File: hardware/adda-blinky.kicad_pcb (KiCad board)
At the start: 2 copper layers, 46.2 x 35.1 mm, 17 parts, among them J1 Conn_01x02, J2 Conn_01x02, J3 USB_B_Micro, J4 Conn_01x02, U1 ATtiny1616-S, U2 ATtiny1616-M, U3 AMS1117-3.3

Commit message: First order
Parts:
- removed C2: 1u, Capacitor_SMD:C_0805_2012Metric
- removed U1: ATtiny1616-S, Package_SO:SOIC-20W_7.5x12.8mm_P1.27mm
- removed U3: AMS1117-3.3, Package_TO_SOT_SMD:SOT-223-3_TabPin2
- added C5: 1u, Capacitor_SMD:C_0805_2012Metric, F.Cu at (120.9, 52.1)
- added D10: 1N5819, Diode_SMD:D_SOD-323, F.Cu at (120.9, 50.0)
- added H1: MountingHole, MountingHole:MountingHole_3.2mm_M3_Pad, F.Cu at (92.7, 41.9)
- added H2: MountingHole, MountingHole:MountingHole_3.2mm_M3_Pad, F.Cu at (92.7, 72.4)
- added H3: MountingHole, MountingHole:MountingHole_3.2mm_M3_Pad, F.Cu at (135.9, 72.4)
- added H4: MountingHole, MountingHole:MountingHole_3.2mm_M3_Pad, F.Cu at (135.9, 41.9)
- added J5: PWR, Connector_Molex:Molex_KK-254_AE-6410-03A_1x03_P2.54mm_Vertical, F.Cu at (123.2, 41.9)
- added R0: 220, Resistor_SMD:R_0805_2012Metric, F.Cu at (121.9, 67.6)
- added R1: 220, Resistor_SMD:R_0805_2012Metric, F.Cu at (119.9, 67.6)
- added R2: 220, Resistor_SMD:R_0805_2012Metric, F.Cu at (117.9, 67.6)
- added R3: 220, Resistor_SMD:R_0805_2012Metric, F.Cu at (115.8, 67.6)
- added R4: 220, Resistor_SMD:R_0805_2012Metric, F.Cu at (113.8, 67.6)
- added R5: 220, Resistor_SMD:R_0805_2012Metric, F.Cu at (111.7, 67.6)
- added R6: 220, Resistor_SMD:R_0805_2012Metric, F.Cu at (109.7, 67.6)
- added R7: 220, Resistor_SMD:R_0805_2012Metric, F.Cu at (107.7, 67.6)
- added R8: 220, Resistor_SMD:R_0805_2012Metric, F.Cu at (125.9, 50.0)
- added RV1: R_Potentiometer, Connector_PinHeader_2.54mm:PinHeader_1x03_P2.54mm_Vertical, F.Cu at (132.1, 48.3)
- J1: value Conn_01x02 -> AIN
- J2: value Conn_01x02 -> AOUT
- J3: value USB_B_Micro -> PB5; footprint Connector_USB:USB_Micro-AB_Molex_47590-0001 -> Connector_Molex:Molex_KK-254_AE-6410-02A_1x02_P2.54mm_Vertical
- J4: value Conn_01x02 -> COMM; footprint Connector_Molex:Molex_KK-254_AE-6410-02A_1x02_P2.54mm_Vertical -> Connector_Molex:Molex_KK-254_AE-6410-05A_1x05_P2.54mm_Vertical
- moved J2 32.1 mm to (135.9, 59.7), turned to -90 degrees
- moved J3 29.4 mm to (115.6, 41.9), turned to 0 degrees
- moved J1 12.3 mm to (92.7, 62.2)
- moved U2 11.8 mm to (115.6, 53.3)
- moved C1 11.4 mm to (125.9, 52.1), turned to 180 degrees
- moved J4 10.7 mm to (100.3, 41.9), turned to 0 degrees
- moved D2 7.39 mm to (117.9, 71.1)
- moved D3 7.39 mm to (115.9, 71.1)
- moved D6 7.39 mm to (109.8, 71.1)
- moved D7 7.39 mm to (107.7, 71.1)
- moved D4 7.39 mm to (113.8, 71.1)
- moved D5 7.39 mm to (111.8, 71.1)
- moved D0 7.38 mm to (121.9, 71.1)
- moved D1 7.38 mm to (119.9, 71.1)
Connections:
- C1 pad 1: +3.3V -> /PB4
- D0 pad 1: /PC0 -> Net-(D0-K)
- D0 pad 2: +3.3V -> +5V
- D1 pad 1: /PC1 -> Net-(D1-K)
- D1 pad 2: +3.3V -> +5V
- D2 pad 1: /PC2 -> Net-(D2-K)
- D2 pad 2: +3.3V -> +5V
- D3 pad 1: /PC3 -> Net-(D3-K)
- D3 pad 2: +3.3V -> +5V
- D4 pad 1: /PB0 -> Net-(D4-K)
- D4 pad 2: +3.3V -> +5V
- D5 pad 1: /PB1 -> Net-(D5-K)
- D5 pad 2: +3.3V -> +5V
- D6 pad 1: /PB2 -> Net-(D6-K)
- D6 pad 2: +3.3V -> +5V
- D7 pad 1: /PB3 -> Net-(D7-K)
- D7 pad 2: +3.3V -> +5V
- J1 pad 1: /PA5/AIN5 -> GND
- J1 pad 2: GND -> /PA5/AIN5
- J3 pad 1: Net-(D8-A) -> GND
- J3 pad 2: unconnected-(J3-D--Pad2) -> /PB5
- J4 pad 1: +VDC -> GND
- J4 pad 2: GND -> /PA4/SS
- U2 pad 4: +3.3V -> +5V
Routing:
- net +5V: track 0.00 -> 60.0 mm, vias 0 -> 2
- net /PA6/OUT: track 3.82 -> 30.1 mm, vias 0 -> 2
- net /PB4: track 3.76 -> 24.2 mm, vias 0 -> 2
- net /PA5/AIN5: track 4.46 -> 24.4 mm
- net /PB5: track 3.42 -> 17.7 mm, vias 0 -> 4
- net /PA4/SS: track 5.72 -> 18.3 mm
- net /PA3/SCK: track 5.69 -> 16.6 mm
- net /PA1/MOSI/SDA: track 3.55 -> 13.6 mm
- net /PA2/MISO/SCL: track 4.59 -> 14.5 mm
- net /~{RESET}: track 3.19 -> 12.7 mm, vias 0 -> 2
- net /UPDI: track 0.00 -> 8.74 mm
- net Net-(D10-A): track 0.00 -> 8.65 mm
- net +3.3V: track 7.77 -> 0.00 mm
- net GND: track 10.9 -> 5.69 mm
- net /PA7: track 3.46 -> 0.00 mm
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- added copper zone on B.Cu, net GND
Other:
- board size 46.2 x 35.1 mm -> 50.8 x 38.1 mm
- board text added: "0"
- board text added: "1"
- board text added: "2"
- board text added: "3"
- board text added: "4"
- board text added: "5"
- board text added: "6"
- board text added: "7"
- board text added: "ADC"
- board text added: "DAC"
- board text added: "GND"
- board text added: "PA1/MOSI/SDA"
- board text added: "PA2/MISO/SCL"
- board text added: "PA3/SCK"
- board text added: "PA4/SS"
- board text added: "PB5"
- board text added: "UPDI"
- board text added: "VDD"
- board text added: "Vin"
- board text added: "Vout"

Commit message: Add series resistors to I/Os
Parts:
- added R10: 220, Resistor_SMD:R_0805_2012Metric, F.Cu at (135.5, 57.1)
- added R9: 220, Resistor_SMD:R_0805_2012Metric, F.Cu at (93.0, 57.1)
- moved J1 1.27 mm to (92.7, 63.5)
- moved J2 1.27 mm to (135.9, 61.0)
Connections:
- J1 pad 2: /PA5/AIN5 -> Net-(J1-Pin_2)
- J2 pad 1: /PA6/OUT -> Net-(J2-Pin_1)
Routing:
- net Net-(J1-Pin_2): track 0.00 -> 4.08 mm
- net Net-(J2-Pin_1): track 0.00 -> 4.03 mm
- net /PB3: track 15.0 -> 17.6 mm
- net /PA6/OUT: track 30.1 -> 27.7 mm
- net /PB2: track 14.1 -> 16.0 mm
- net /PA5/AIN5: track 24.4 -> 22.5 mm
- net GND: track 5.69 -> 7.03 mm, vias 3 -> 4
- net /PB1: track 13.5 -> 14.4 mm
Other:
- board text added: "8b"

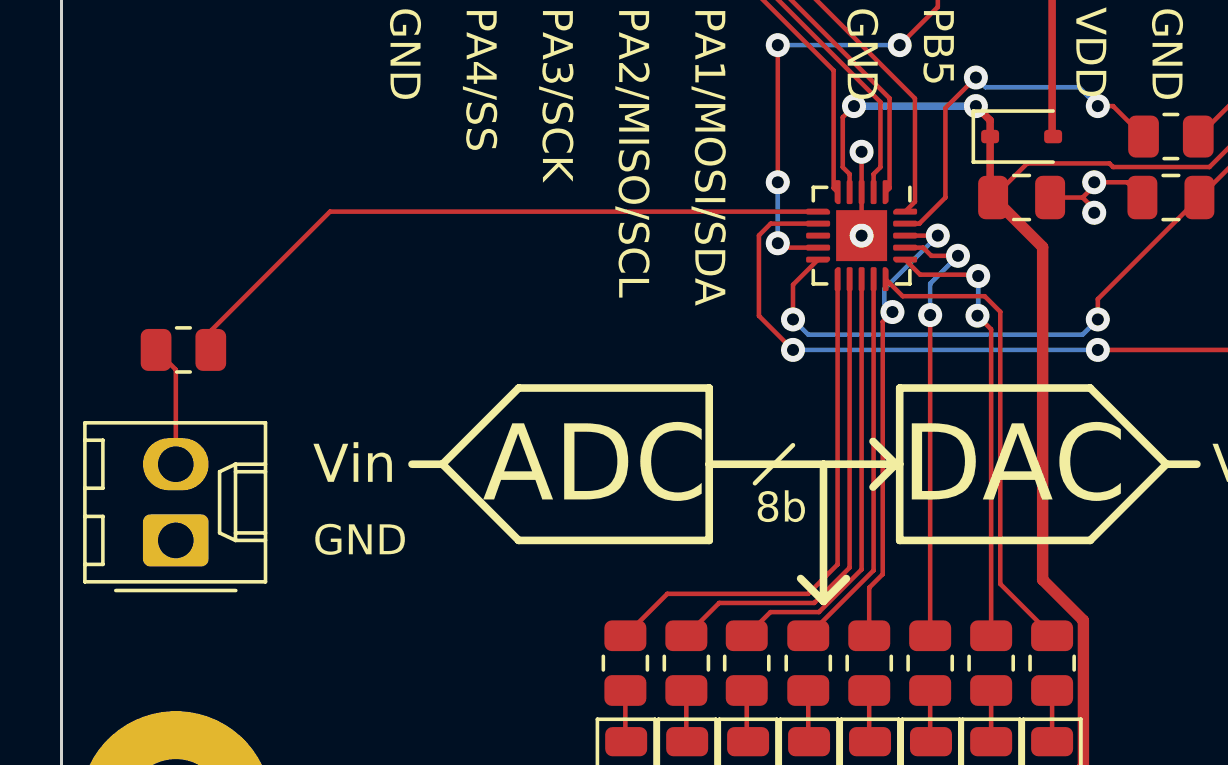
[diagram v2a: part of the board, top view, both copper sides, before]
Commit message: Add LED to PB5 for status and sample indicator
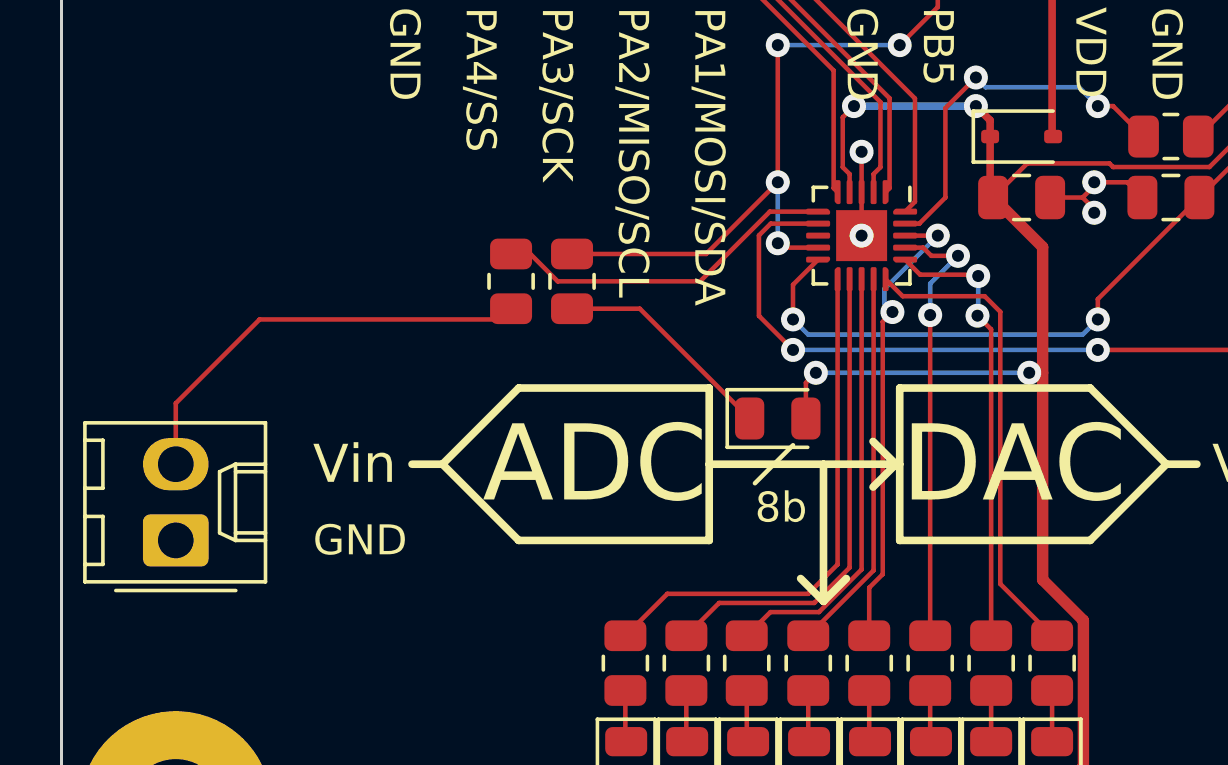
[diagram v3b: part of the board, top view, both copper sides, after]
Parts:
- added D8: LED, Diode_SMD:D_0805_2012Metric, F.Cu at (112.8, 59.4)
- added R11: 220, Resistor_SMD:R_0805_2012Metric, F.Cu at (105.9, 54.9)
- RV1: value R_Potentiometer -> FS
- moved R9 11.2 mm to (103.9, 54.9), turned to 90 degrees
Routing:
- net /PA5/AIN5: track 22.5 -> 11.6 mm
- net Net-(J1-Pin_2): track 4.08 -> 14.5 mm
- net +5V: track 60.2 -> 69.4 mm, vias 2 -> 4
- net /PB5: track 17.7 -> 25.5 mm
- net Net-(D8-K): track 0.00 -> 7.44 mm

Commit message: Swap LED orientation
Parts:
- moved D8 0.25 mm to (112.8, 59.2), turned to 180 degrees
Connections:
- D8 pad 1: Net-(D8-K) -> GND
- D8 pad 2: +5V -> Net-(D8-A)
- R11 pad 2: Net-(D8-K) -> Net-(D8-A)
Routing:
- net +5V: track 69.4 -> 60.2 mm, vias 4 -> 2
- net Net-(D8-A): track 0.00 -> 7.54 mm
- net Net-(D8-K): track 7.44 -> 0.00 mm
- net GND: track 7.03 -> 8.22 mm, vias 4 -> 5
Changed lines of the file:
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@@
   (net 31 "Net-(J1-Pin_2)")
   (net 32 "Net-(J2-Pin_1)")
-  (net 33 "Net-(D8-K)")
+  (net 33 "Net-(D8-A)")
   (footprint "Connector_Molex:Molex_KK-254_AE-6410-02A_1x02_P2.54mm_Vertical" locked (layer "F.Cu")
     (at 92.71 63.5 90)
@@
       (net 2 "/PB5") (pintype "passive"))
     (pad "2" smd roundrect (at 0.9125 0 270) (size 1.025 1.4) (layers "F.Cu" "F.Paste" "F.Mask") (roundrect_rratio 0.243902439)
-      (net 33 "Net-(D8-K)") (pintype "passive"))
+      (net 33 "Net-(D8-A)") (pintype "passive"))
     (model "${KICAD6_3DMODEL_DIR}/Resistor_SMD.3dshapes/R_0805_2012Metric.wrl"
       (offset (xyz 0 0 0))
@@
   )
   (footprint "Diode_SMD:D_0805_2012Metric" (layer "F.Cu")
-    (at 112.776 59.436)
+    (at 112.776 59.182 180)
     (descr "Diode SMD 0805 (2012 Metric), square (rectangular) end terminal, IPC_7351 nominal, (Body size source: https://docs.google.com/spreadsheets/d/1BsfQQcO9C6DZCsRaXUlFlo91Tg2WpOkGARC1WS5S8t0/edit?usp=sharing), generated with kicad-footprint-generator")
     (tags "diode")
@@
     (fp_line (start 1 0.6) (end 1 -0.6)
       (stroke (width 0.1) (type solid)) (layer "F.Fab"))
-    (pad "1" smd roundrect (at -0.9375 0) (size 0.975 1.4) (layers "F.Cu" "F.Paste" "F.Mask") (roundrect_rratio 0.25)
-      (net 33 "Net-(D8-K)") (pinfunction "K") (pintype "passive"))
-    (pad "2" smd roundrect (at 0.9375 0) (size 0.975 1.4) (layers "F.Cu" "F.Paste" "F.Mask") (roundrect_rratio 0.25)
-      (net 12 "+5V") (pinfunction "A") (pintype "passive"))
+    (pad "1" smd roundrect (at -0.9375 0 180) (size 0.975 1.4) (layers "F.Cu" "F.Paste" "F.Mask") (roundrect_rratio 0.25)
+      (net 13 "GND") (pinfunction "K") (pintype "passive"))
+    (pad "2" smd roundrect (at 0.9375 0 180) (size 0.975 1.4) (layers "F.Cu" "F.Paste" "F.Mask") (roundrect_rratio 0.25)
+      (net 33 "Net-(D8-A)") (pinfunction "A") (pintype "passive"))
     (model "${KICAD6_3DMODEL_DIR}/Diode_SMD.3dshapes/D_0805_2012Metric.wrl"
       (offset (xyz 0 0 0))
@@
     (property "ki_description" "Mounting Hole without connection")
     (property "ki_keywords" "mounting hole")
-    (attr exclude_from_pos_files)
+    (attr exclude_from_pos_files exclude_from_bom)
     (fp_text reference "H1" (at 0 -4.2) (layer "F.SilkS") hide
         (effects (font (size 1 1) (thickness 0.15)))
@@
   (segment (start 119.854 50.038) (end 119.854 51.97) (width 0.254) (layer "F.Cu") (net 12))
   (segment (start 121.0906 50.9334) (end 119.954 52.07) (width 0.1524) (layer "F.Cu") (net 12))
-  (segment (start 113.7135 59.436) (end 113.7135 58.2445) (width 0.1524) (layer "F.Cu") (net 12))
   (segment (start 123.8314 50.9334) (end 121.0906 50.9334) (width 0.1524) (layer "F.Cu") (net 12))
   (segment (start 119.854 51.97) (end 119.954 52.07) (width 0.1524) (layer "F.Cu") (net 12))
@@
   (segment (start 121.604902 57.912) (end 121.604902 64.811415) (width 0.381) (layer "F.Cu") (net 12))
   (segment (start 127.166343 51.054) (end 123.952 51.054) (width 0.1524) (layer "F.Cu") (net 12))
-  (segment (start 113.7135 58.2445) (end 114.046 57.912) (width 0.1524) (layer "F.Cu") (net 12))
-  (segment (start 121.158 57.912) (end 121.604902 57.912) (width 0.1524) (layer "F.Cu") (net 12))
   (segment (start 122.9629 71.0406) (end 121.92 72.0835) (width 0.381) (layer "F.Cu") (net 12))
   (via (at 119.38 49.022) (size 0.8) (drill 0.4) (layers "F.Cu" "B.Cu") (net 12))
   (via (at 115.316 49.022) (size 0.8) (drill 0.4) (layers "F.Cu" "B.Cu") (net 12))
-  (via (at 121.158 57.912) (size 0.8) (drill 0.4) (layers "F.Cu" "B.Cu") (net 12))
-  (via (at 114.046 57.912) (size 0.8) (drill 0.4) (layers "F.Cu" "B.Cu") (net 12))
-  (segment (start 114.046 57.912) (end 121.158 57.912) (width 0.1524) (layer "B.Cu") (net 12))
   (segment (start 119.38 49.022) (end 115.316 49.022) (width 0.254) (layer "B.Cu") (net 12))
   (segment (start 124.4225 51.562) (end 123.3239 51.562) (width 0.1524) (layer "F.Cu") (net 13))
@@
   (segment (start 122.936 52.07) (end 123.3239 51.6821) (width 0.1524) (layer "F.Cu") (net 13))
   (segment (start 115.57 51.89) (end 115.57 50.546) (width 0.1524) (layer "F.Cu") (net 13))
+  (segment (start 113.7135 58.5944) (end 114.1419 58.166) (width 0.1524) (layer "F.Cu") (net 13))
   (segment (start 123.3239 51.6821) (end 123.3239 51.562) (width 0.1524) (layer "F.Cu") (net 13))
   (segment (start 123.3239 52.4579) (end 123.3239 52.578) (width 0.1524) (layer "F.Cu") (net 13))
+  (segment (start 113.7135 59.182) (end 113.7135 58.5944) (width 0.1524) (layer "F.Cu") (net 13))
   (segment (start 122.936 52.07) (end 121.854 52.07) (width 0.1524) (layer "F.Cu") (net 13))
   (segment (start 115.57 51.89) (end 115.57 53.34) (width 0.1524) (layer "F.Cu") (net 13))
   (via (at 123.3239 51.562) (size 0.8) (drill 0.4) (layers "F.Cu" "B.Cu") (net 13))
   (via (at 115.57 53.34) (size 0.8) (drill 0.4) (layers "F.Cu" "B.Cu") (net 13))
+  (via (at 114.1419 58.166) (size 0.8) (drill 0.4) (layers "F.Cu" "B.Cu") (net 13))
   (via (at 123.3239 52.578) (size 0.8) (drill 0.4) (layers "F.Cu" "B.Cu") (net 13))
   (via (at 115.57 50.546) (size 0.8) (drill 0.4) (layers "F.Cu" "B.Cu") (net 13))
@@
   (segment (start 135.89 59.69) (end 136.4215 59.1585) (width 0.1524) (layer "F.Cu") (net 32))
   (segment (start 136.4215 57.15) (end 136.4215 59.1585) (width 0.1524) (layer "F.Cu") (net 32))
-  (segment (start 111.8385 59.436) (end 108.179 55.7765) (width 0.1524) (layer "F.Cu") (net 33))
-  (segment (start 108.179 55.7765) (end 105.918 55.7765) (width 0.1524) (layer "F.Cu") (net 33))
+  (segment (start 110.3145 57.658) (end 107.442 57.658) (width 0.1524) (layer "F.Cu") (net 33))
+  (segment (start 107.442 57.658) (end 105.918 56.134) (width 0.1524) (layer "F.Cu") (net 33))
+  (segment (start 105.918 56.134) (end 105.918 55.7765) (width 0.1524) (layer "F.Cu") (net 33))
+  (segment (start 111.8385 59.182) (end 110.3145 57.658) (width 0.1524) (layer "F.Cu") (net 33))
   (zone (net 13) (net_name "GND") (layer "B.Cu") (hatch edge 0.5)
     (connect_pads (clearance 0.508))
